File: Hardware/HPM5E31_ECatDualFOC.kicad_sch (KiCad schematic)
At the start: 5 parts, among them U34 M3, U38 M3, U46 M3, U47 M3

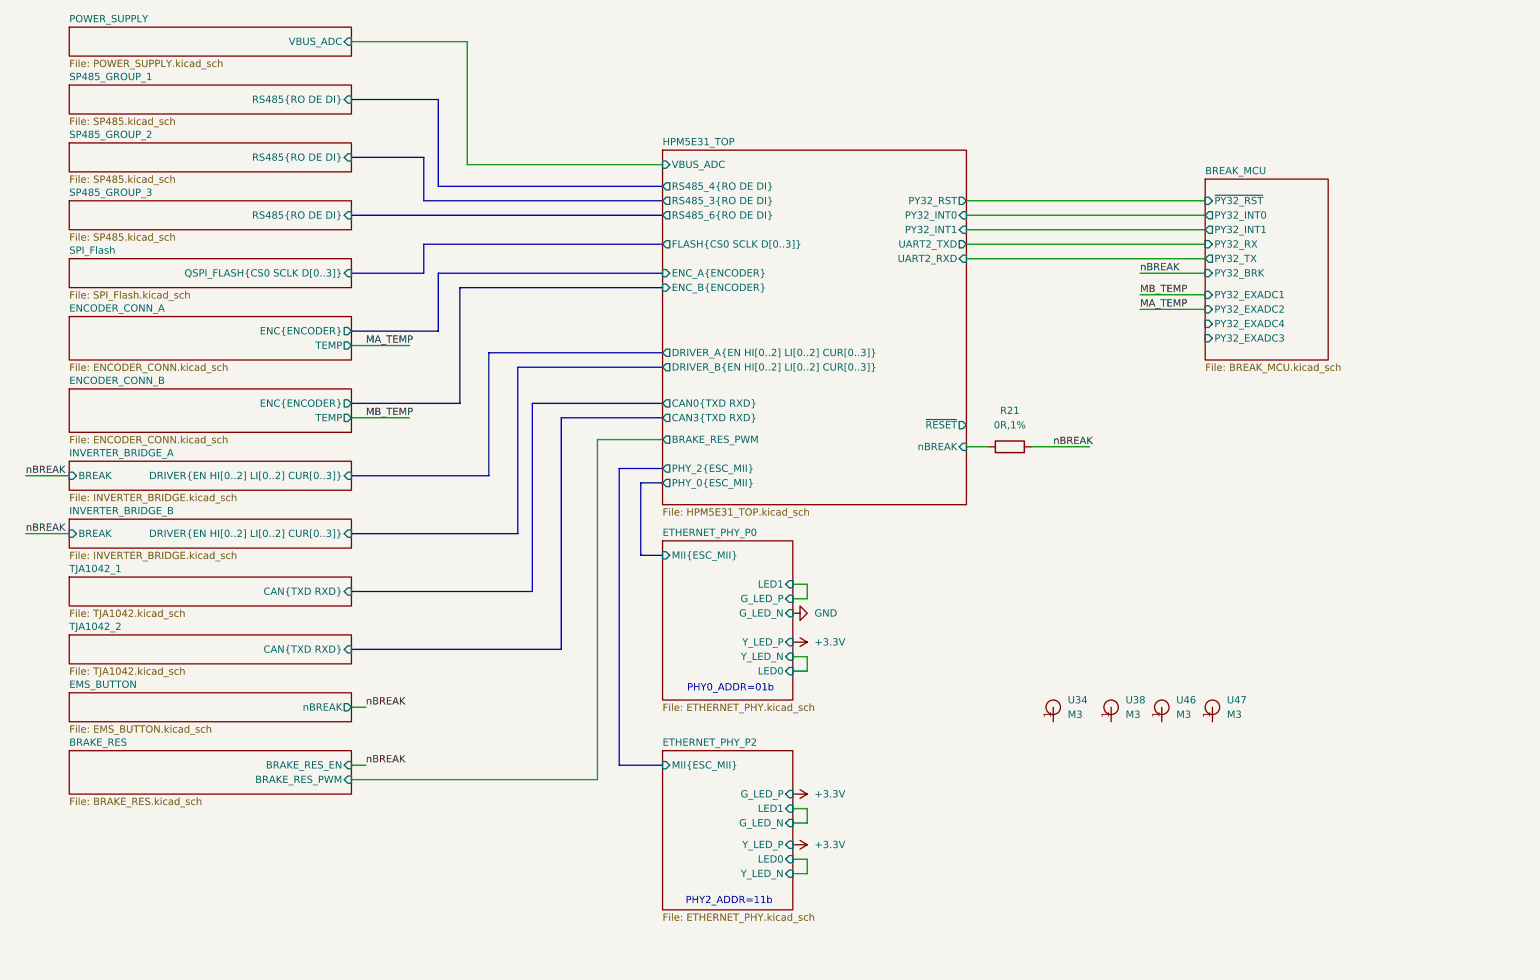
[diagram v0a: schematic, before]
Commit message: PCB：网口替换为HR911205C
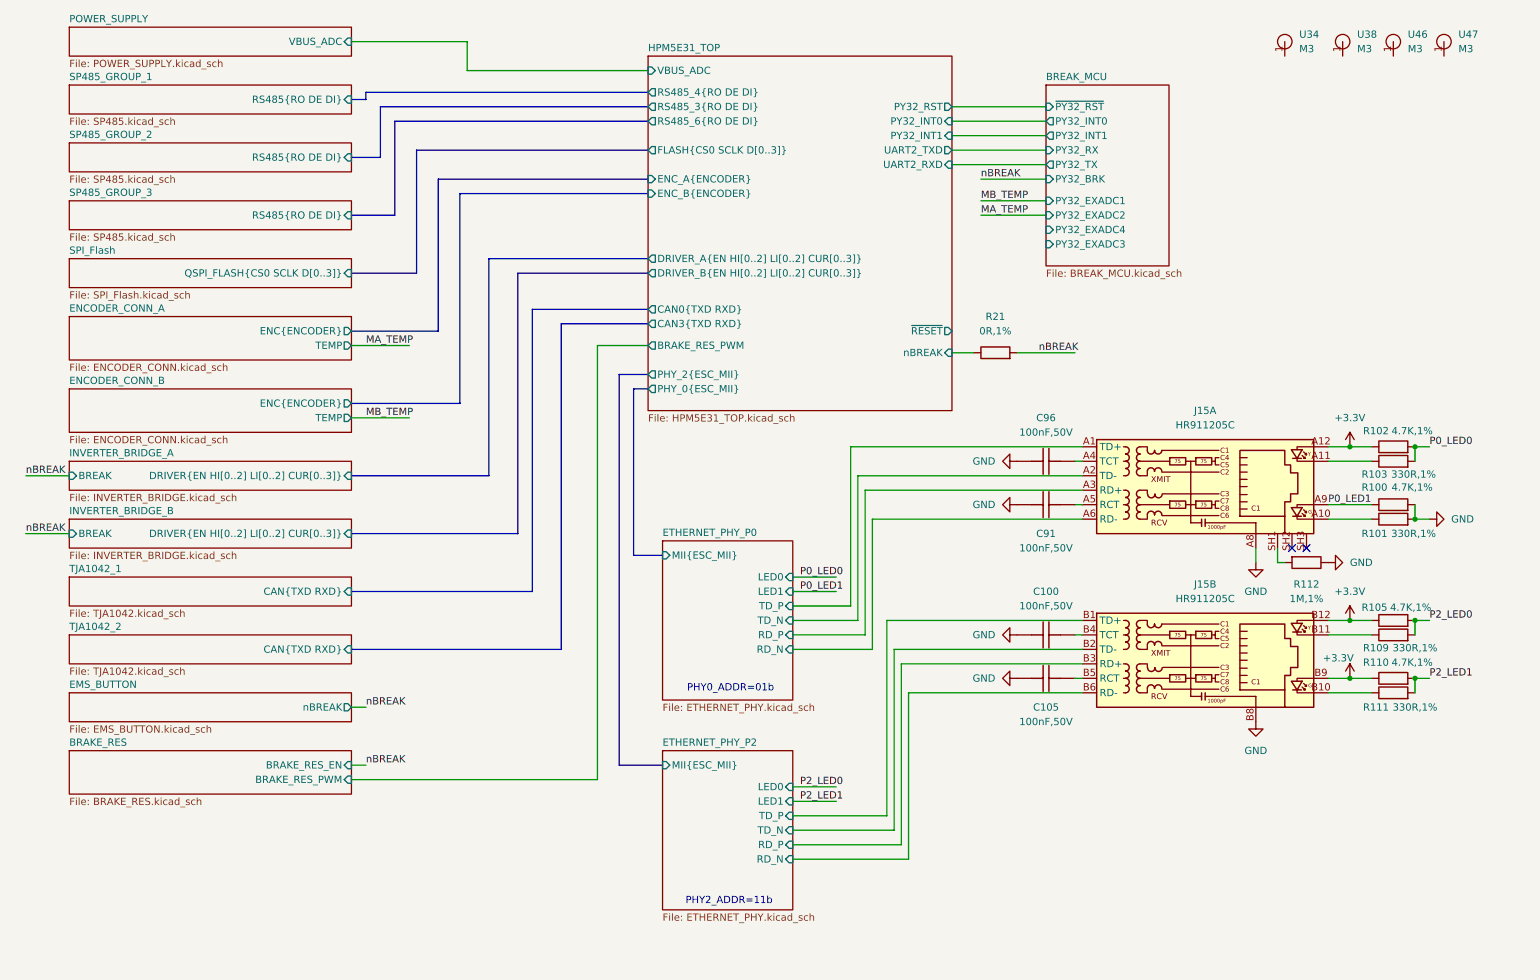
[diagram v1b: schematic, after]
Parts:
- added C100, C105, C91, C96: 100nF,50V, Capacitor_SMD:C_0603_1608Metric, symbol HPM6280Foc:CC0603KRX7R9BB104
- added J15: HR911205C, Library:HR911205C, symbol HPM6280Foc:HR911205C
- added R100, R102, R105, R110: 4.7K,1%, Resistor_SMD:R_0402_1005Metric, symbol HPM6280Foc:0402WGF4701TCE
- added R101, R103, R109, R111: 330R,1%, Resistor_SMD:R_0402_1005Metric, symbol HPM6280Foc:0402WGF3300TCE
- added R112: 1M,1%, Resistor_SMD:R_0805_2012Metric, symbol HPM6280Foc:0805W8F1004T5E
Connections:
- net +3.3V: now also J15.A12, J15.B12, J15.B9, R102.1, R105.1, R110.1
- net GND: now also C100.2, C105.2, C91.2, C96.2, J15.A8, J15.B8, R100.2, R101.2, R112.1
- new net: C91.1, J15.A5 (RCT)
- new net: J15.A10, R101.1
- new net: J15.A11, R103.1
- new net: C96.1, J15.A4 (TCT)
- new net: J15.SH1, R112.2
- new net: J15.B10, R111.1
- new net: J15.B11, R109.1
- new net: C100.1, J15.B4 (TCT)
- new net: C105.1, J15.B5 (RCT)
- new net ETHERNET_PHY_P0/RD_N: J15.A6 (RD-)
- new net ETHERNET_PHY_P0/RD_P: J15.A3 (RD+)
- new net ETHERNET_PHY_P0/TD_N: J15.A2 (TD-)
- new net ETHERNET_PHY_P0/TD_P: J15.A1 (TD+)
- new net ETHERNET_PHY_P2/RD_N: J15.B6 (RD-)
- new net ETHERNET_PHY_P2/RD_P: J15.B3 (RD+)
- new net ETHERNET_PHY_P2/TD_N: J15.B2 (TD-)
- new net ETHERNET_PHY_P2/TD_P: J15.B1 (TD+)
- new net P0_LED0: R102.2, R103.2
- new net P0_LED1: J15.A9, R100.1
- new net P2_LED0: R105.2, R109.2
- new net P2_LED1: R110.2, R111.2
- no-connect marks 0 -> 2
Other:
- sheet ETHERNET_PHY_P0 ports: added RD_N, RD_P, TD_N, TD_P; removed G_LED_N, G_LED_P, Y_LED_N, Y_LED_P
- sheet ETHERNET_PHY_P2 ports: added RD_N, RD_P, TD_N, TD_P; removed G_LED_N, G_LED_P, Y_LED_N, Y_LED_P
- moved on the sheet: R21, U34, U38, U46, U47

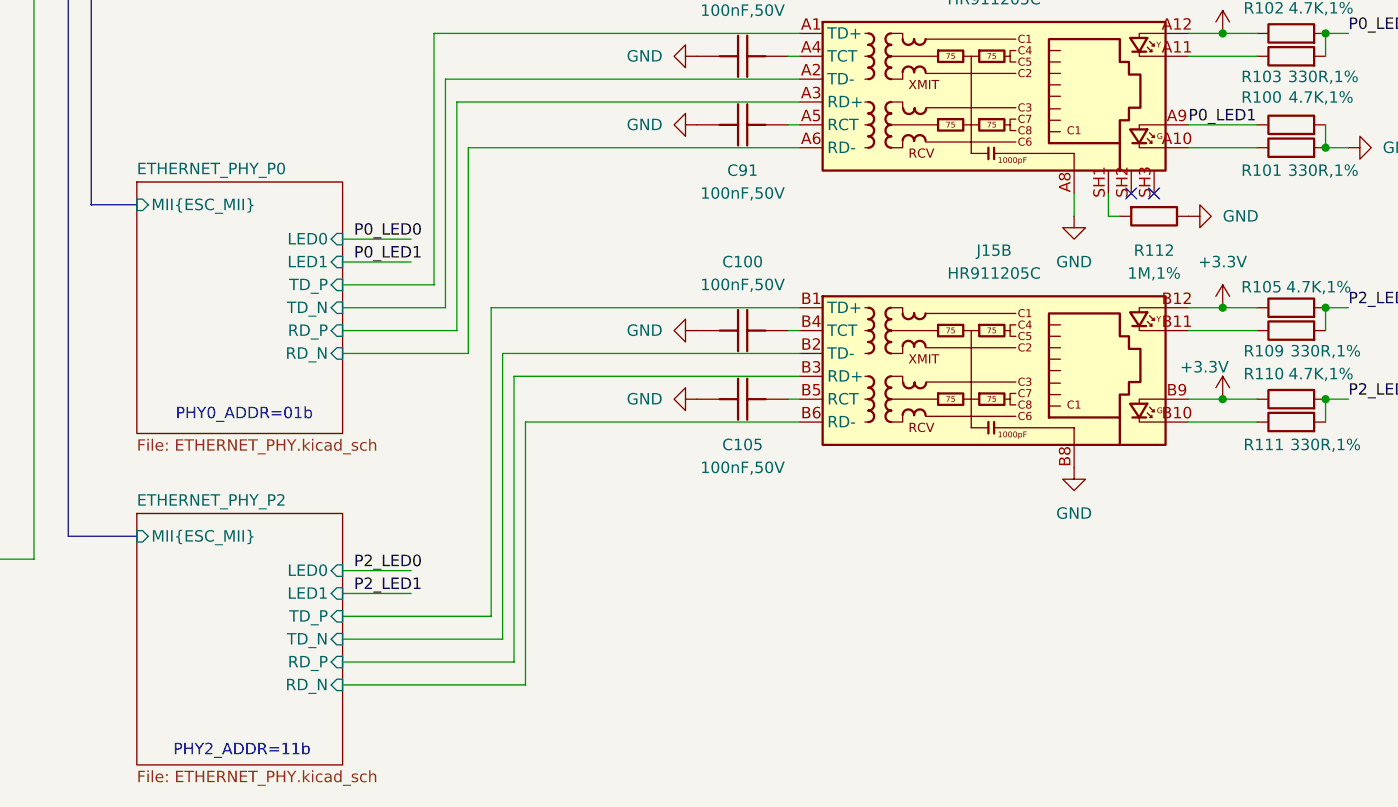
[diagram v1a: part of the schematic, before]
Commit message: 更改网口接地，更改RC吸收封装
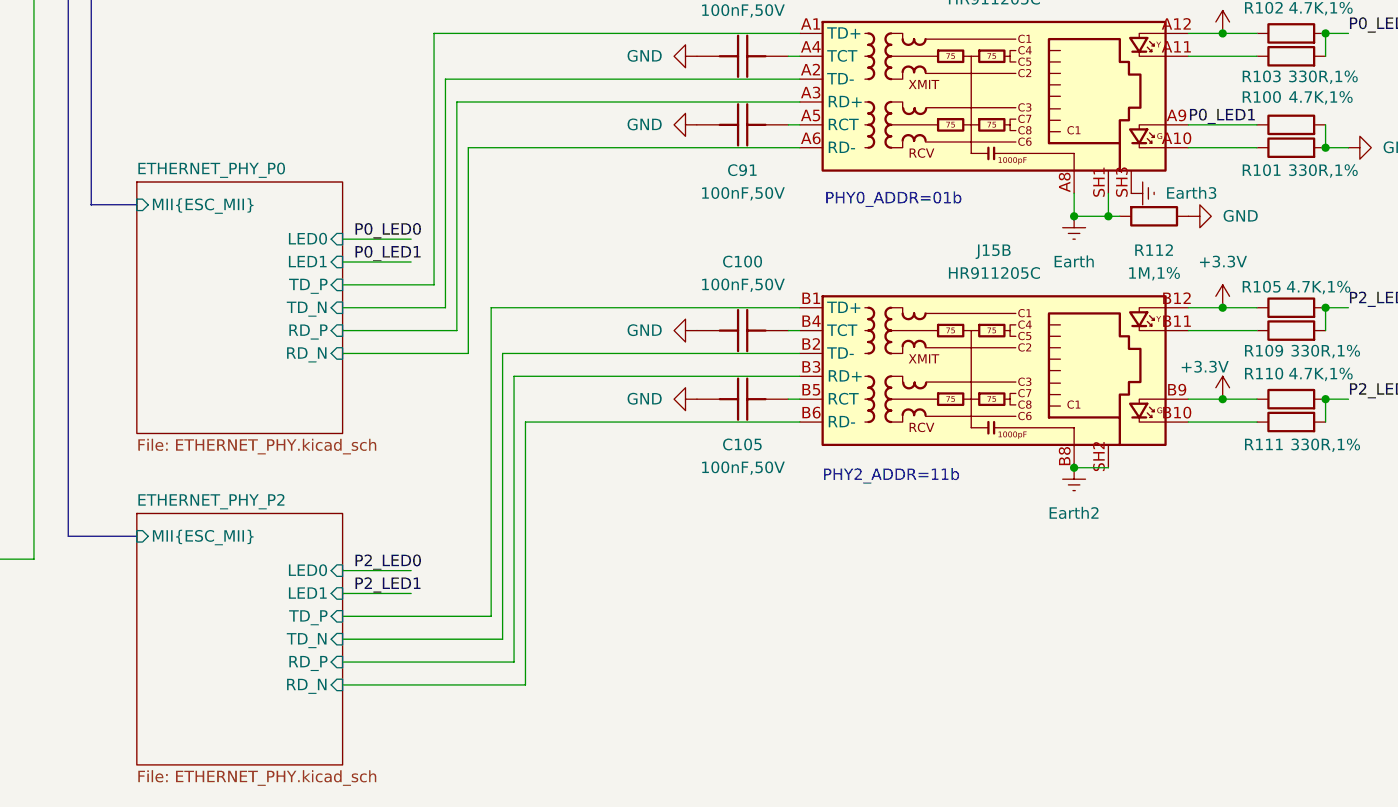
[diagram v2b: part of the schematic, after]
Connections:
- net GND: no longer J15.A8, J15.B8
- net Earth: now reaches J15.SH1, R112.2
- net Earth: now also J15.A8
- net Earth3: now reaches J15.SH3
- new net Earth2: J15.B8, J15.SH2
- no-connect marks 2 -> 0
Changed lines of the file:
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@@
 	(text "PHY2_ADDR=11b"
 		(exclude_from_sim no)
-		(at 141.224 186.436 0)
+		(at 213.36 155.956 0)
 		(effects
 			(font
@@
 	(text "PHY0_ADDR=01b"
 		(exclude_from_sim no)
-		(at 141.478 149.098 0)
+		(at 213.614 125.222 0)
 		(effects
 			(font
@@
 	)
 	(junction
+		(at 237.49 127)
+		(diameter 0)
+		(color 0 0 0 0)
+	)
+	(junction
 		(at 261.62 119.38)
 		(diameter 0)
@@
 	)
 	(junction
+		(at 233.68 127)
+		(diameter 0)
+		(color 0 0 0 0)
+	)
+	(junction
 		(at 261.62 106.68)
 		(diameter 0)
@@
 	)
 	(junction
+		(at 233.68 154.94)
+		(diameter 0)
+		(color 0 0 0 0)
+	)
+	(junction
 		(at 250.19 147.32)
 		(diameter 0)
@@
 		(color 0 0 0 0)
 	)
-	(no_connect
-		(at 240.03 124.46)
-	)
-	(no_connect
-		(at 242.57 124.46)
-	)
 	(wire
 		(pts
@@
 		)
 	)
+	(wire
+		(pts
+			(xy 233.68 154.94) (xy 237.49 154.94)
+		)
+		(stroke
+			(width 0)
+			(type default)
+		)
+	)
 	(bus
 		(pts
@@
 	(wire
 		(pts
+			(xy 233.68 127) (xy 237.49 127)
+		)
+		(stroke
+			(width 0)
+			(type default)
+		)
+	)
+	(wire
+		(pts
 			(xy 180.34 54.61) (xy 196.85 54.61)
 		)
@@
 		(pin "A11"
 		)
-		(pin "SH"
+		(pin "SH1"
 		)
 		(pin "A10"
@@
 		(pin "A12"
 		)
+		(pin "SH3"
+		)
+		(pin "SH2"
+		)
 		(instances
 			(project ""
@@
 	)
 	(symbol
+		(lib_id "power:Earth")
+		(at 240.03 124.46 90)
+		(unit 1)
+		(exclude_from_sim no)
+		(in_bom yes)
+		(on_board yes)
+		(dnp no)
+		(fields_autoplaced yes)
+		(property "Reference" "#PWR0356"
+			(at 246.38 124.46 0)
+			(effects
+				(font
+					(size 1.27 1.27)
+				)
+				(hide yes)
+			)
+		)
+		(property "Value" "Earth3"
+			(at 243.84 124.4599 90)
+			(effects
+				(font
+					(size 1.27 1.27)
+				)
+				(justify right)
+			)
+		)
+		(property "Footprint" ""
+			(at 240.03 124.46 0)
+			(effects
+				(font
+					(size 1.27 1.27)
+				)
+				(hide yes)
+			)
+		)
+		(property "Datasheet" "~"
+			(at 240.03 124.46 0)
+			(effects
+				(font
+					(size 1.27 1.27)
+				)
+				(hide yes)
+			)
+		)
+		(property "Description" "Power symbol creates a global label with name \"Earth\""
+			(at 240.03 124.46 0)
+			(effects
+				(font
+					(size 1.27 1.27)
+				)
+				(hide yes)
+			)
+		)
+		(pin "1"
+		)
+		(instances
+			(project "HPM5E31_ECatDualFOC"
+				(path "/a07e9810-3899-4327-ba8f-f24142a7c70e"
+					(reference "#PWR0356")
+					(unit 1)
+				)
+			)
+		)
+	)
+	(symbol
 		(lib_id "power:+3.3V")
 		(at 250.19 137.16 0)
@@
 	(symbol
 		(lib_id "power:GND")
-		(at 233.68 127 0)
+		(at 191.77 147.32 270)
 		(unit 1)
 		(exclude_from_sim no)
@@
 		(dnp no)
 		(fields_autoplaced yes)
-		(property "Reference" "#PWR0254"
-			(at 233.68 133.35 0)
+		(property "Reference" "#PWR0219"
+			(at 185.42 147.32 0)
 			(effects
 				(font
@@
 		)
 		(property "Value" "GND"
-			(at 233.68 132.08 0)
+			(at 187.96 147.3199 90)
 			(effects
 				(font
 					(size 1.27 1.27)
 				)
+				(justify right)
 			)
 		)
 		(property "Footprint" ""
-			(at 233.68 127 0)
+			(at 191.77 147.32 0)
 			(effects
 				(font
@@
 		)
 		(property "Datasheet" ""
-			(at 233.68 127 0)
+			(at 191.77 147.32 0)
 			(effects
 				(font
@@
 		)
 		(property "Description" "Power symbol creates a global label with name \"GND\" , ground"
-			(at 233.68 127 0)
+			(at 191.77 147.32 0)
 			(effects
 				(font
@@
 			(project "HPM5E31_ECatDualFOC"
 				(path "/a07e9810-3899-4327-ba8f-f24142a7c70e"
-					(reference "#PWR0254")
+					(reference "#PWR0219")
 					(unit 1)
 				)
@@
 	)
 	(symbol
-		(lib_id "power:GND")
-		(at 191.77 147.32 270)
+		(lib_id "power:Earth")
+		(at 233.68 154.94 0)
 		(unit 1)
 		(exclude_from_sim no)
@@
 		(dnp no)
 		(fields_autoplaced yes)
-		(property "Reference" "#PWR0219"
-			(at 185.42 147.32 0)
+		(property "Reference" "#PWR0255"
+			(at 233.68 161.29 0)
 			(effects
 				(font
@@
 			)
 		)
-		(property "Value" "GND"
-			(at 187.96 147.3199 90)
+		(property "Value" "Earth2"
+			(at 233.68 160.02 0)
 			(effects
 				(font
 					(size 1.27 1.27)
 				)
-				(justify right)
 			)
 		)
 		(property "Footprint" ""
-			(at 191.77 147.32 0)
+			(at 233.68 154.94 0)
 			(effects
 				(font
@@
 			)
 		)
-		(property "Datasheet" ""
-			(at 191.77 147.32 0)
+		(property "Datasheet" "~"
+			(at 233.68 154.94 0)
 			(effects
 				(font
@@
 			)
 		)
-		(property "Description" "Power symbol creates a global label with name \"GND\" , ground"
-			(at 191.77 147.32 0)
+		(property "Description" "Power symbol creates a global label with name \"Earth\""
+			(at 233.68 154.94 0)
 			(effects
 				(font
@@
 			(project "HPM5E31_ECatDualFOC"
 				(path "/a07e9810-3899-4327-ba8f-f24142a7c70e"
-					(reference "#PWR0219")
+					(reference "#PWR0255")
 					(unit 1)
 				)
@@
 	)
 	(symbol
-		(lib_id "power:GND")
-		(at 233.68 154.94 0)
+		(lib_id "power:Earth")
+		(at 233.68 127 0)
 		(unit 1)
 		(exclude_from_sim no)
@@
 		(dnp no)
 		(fields_autoplaced yes)
-		(property "Reference" "#PWR0255"
-			(at 233.68 161.29 0)
+		(property "Reference" "#PWR0254"
+			(at 233.68 133.35 0)
 			(effects
 				(font
@@
 			)
 		)
-		(property "Value" "GND"
-			(at 233.68 160.02 0)
+		(property "Value" "Earth"
+			(at 233.68 132.08 0)
 			(effects
 				(font
@@
 		)
 		(property "Footprint" ""
-			(at 233.68 154.94 0)
+			(at 233.68 127 0)
 			(effects
 				(font
@@
 			)
 		)
-		(property "Datasheet" ""
-			(at 233.68 154.94 0)
+		(property "Datasheet" "~"
+			(at 233.68 127 0)
 			(effects
 				(font
@@
 			)
 		)
-		(property "Description" "Power symbol creates a global label with name \"GND\" , ground"
-			(at 233.68 154.94 0)
+		(property "Description" "Power symbol creates a global label with name \"Earth\""
+			(at 233.68 127 0)
 			(effects
 				(font
@@
 		)
 		(instances
-			(project "HPM5E31_ECatDualFOC"
+			(project ""
 				(path "/a07e9810-3899-4327-ba8f-f24142a7c70e"
-					(reference "#PWR0255")
+					(reference "#PWR0254")
 					(unit 1)
 				)
